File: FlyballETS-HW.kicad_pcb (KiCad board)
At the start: 2 copper layers, 94 x 108 mm, 65 parts, among them J1 CONN_01X03, J10 CONN_01X03, J11 CONN_01X03, J12 CONN_01X03, J13 CONN_01X03, J14 CONN_01X03, J15 CONN_01X03, J16 CONN_01X03, J17 CONN_01X03, J18 CONN_01X03, J19 CONN_01X03, J2 CONN_01X03, J20 CONN_01X03, J21 CONN_01X02, J22 CONN_01X02, J23 CONN_01X02, J24 CONN_01X03, J25 CONN_02X09, J26 CONN_01X08, J27 CONN_01X02, J28 Conn_01x04, J3 CONN_01X03, J4 CONN_01X03, J5 CONN_01X03, J6 CONN_01X03, J7 CONN_01X03, J8 CONN_01X03, J9 CONN_01X03, Q1 BC557, Q2 BC557, U1 Wemos_LoLin32, U2 DC-DCStepdown-LM2596

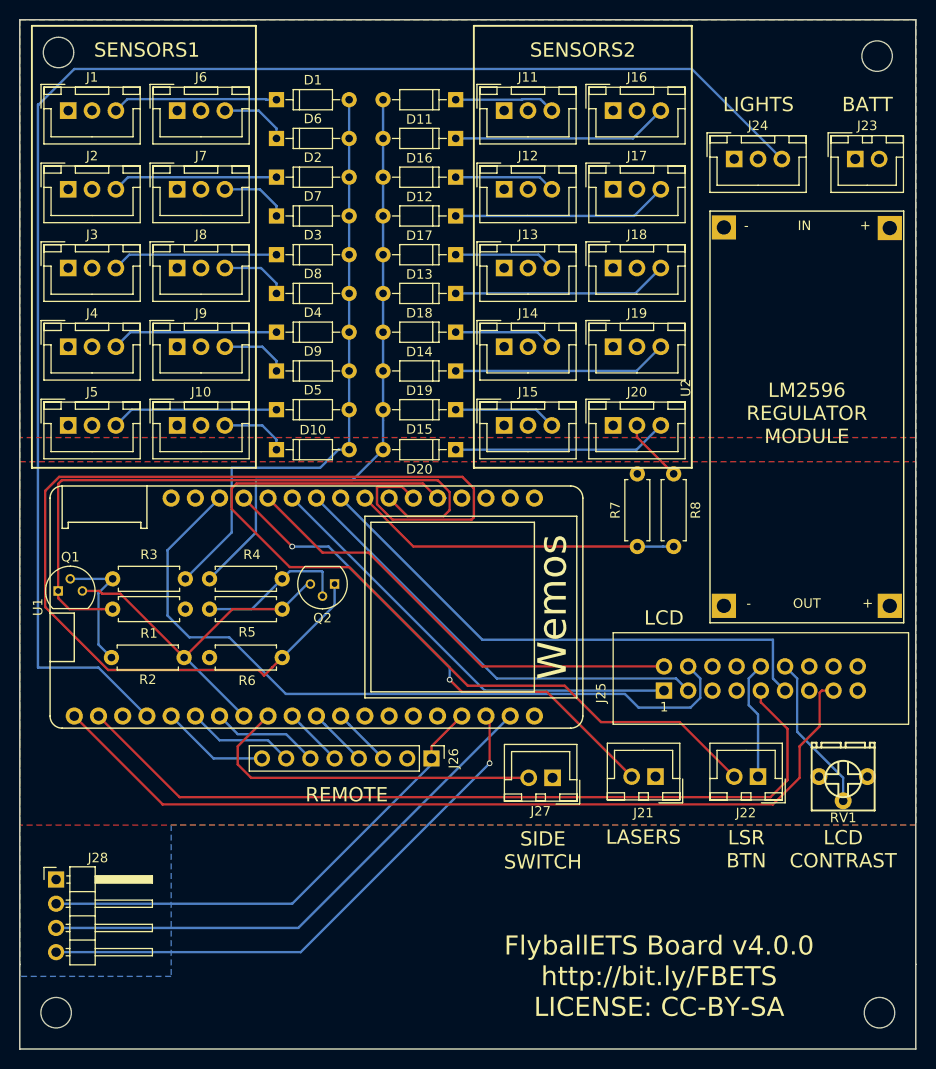
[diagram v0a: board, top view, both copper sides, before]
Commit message: Fixed some prototype problems
- Ran final DRC to fix copper planes (fixes #9)
- R1 pad 1 was connected to GND (fixes #10)
- Changed Q1 and Q2 to TO-92 inline wide footprint (fixes #11)
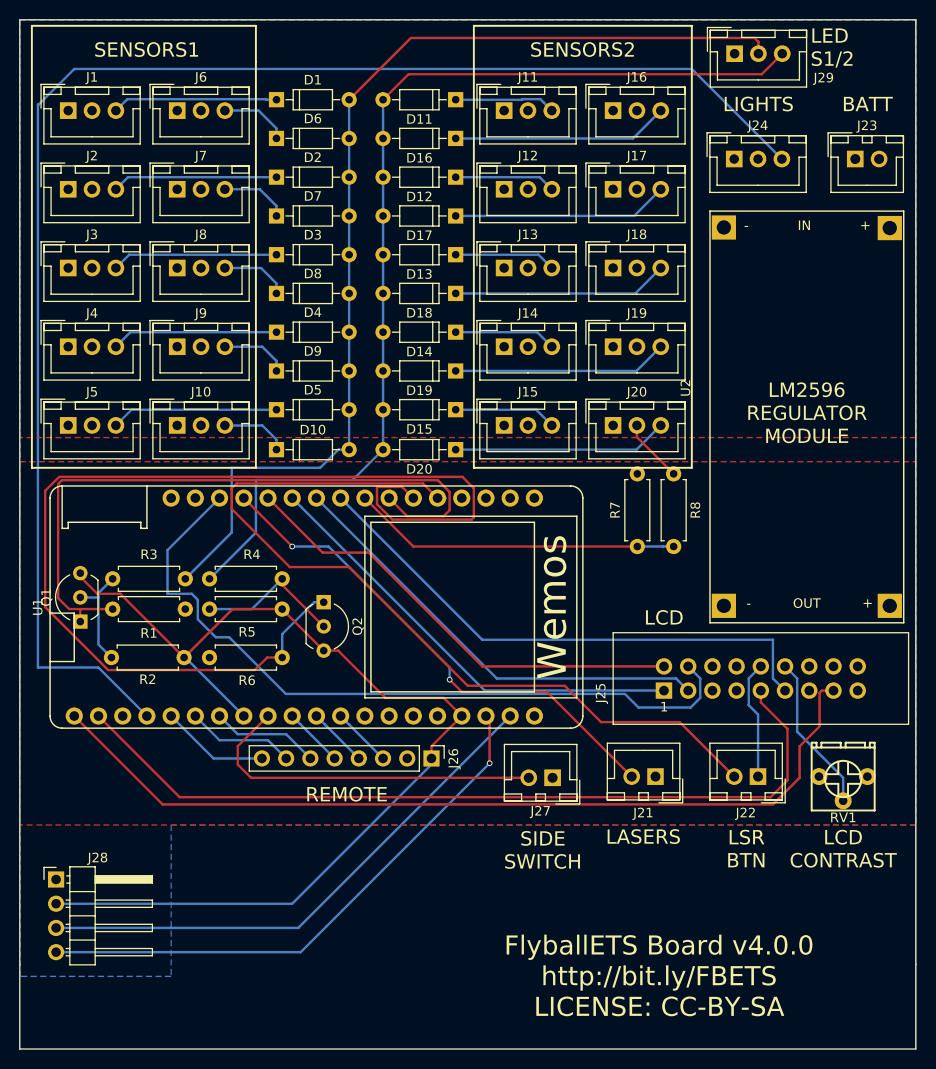
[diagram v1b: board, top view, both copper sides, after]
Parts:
- removed ? (x4): MountingHole_3.2mm_M3, Mounting_Holes:MountingHole_3.2mm_M3
- added J29: CONN_01X03, Connectors_JST:JST_XH_B03B-XH-A_03x2.50mm_Straight, F.Cu at (141.0, 37.8)
- Q1, Q2: footprint TO_SOT_Packages_THT:TO-92_Molded_Narrow -> TO_SOT_Packages_THT:TO-92_Inline_Wide
- moved Q1 3.97 mm to (72.4, 97.4), turned to 90 degrees
- moved Q2 2.22 mm to (97.9, 95.4), turned to 270 degrees
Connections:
- R1 pad 1: Net-(R1-Pad1) -> GND
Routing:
- net S1: track 63.5 -> 110.5 mm
- net S2: track 63.7 -> 107.6 mm
- net +3V3: track 90.7 -> 111.4 mm
- net Net-(Q1-Pad2): track 13.9 -> 11.3 mm
- net S2-IN: track 116.9 -> 114.6 mm
- net S1-IN: track 69.6 -> 71.0 mm
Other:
- board text added: "LED S1/2"
